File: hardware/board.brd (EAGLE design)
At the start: 100 x 100 mm, 131 parts, among them CON2 USB-FPGA-2THT, IC1 THS3062, IC2 AD80XX, U1 AD9215BRUZ, X1 BU-SMA-V

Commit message: Fully routed ADC
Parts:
- moved CD3 188.6 mm to (48.3, 69.0), flipped to the bottom, turned to 270 degrees
- moved CD4 183.7 mm to (50.7, 69.0), flipped to the bottom, turned to 270 degrees
- moved CD2 176.6 mm to (33.5, 65.2), flipped to the bottom
- moved CR4 176.4 mm to (42.8, 63.1), flipped to the bottom, turned to 90 degrees
- moved CR1 172.0 mm to (39.7, 64.6), flipped to the bottom
- moved CD1 168.1 mm to (33.5, 62.9), flipped to the bottom
- moved CR3 167.2 mm to (36.9, 63.6), flipped to the bottom, turned to 270 degrees
- moved CR2 164.5 mm to (39.7, 62.9), flipped to the bottom
- moved CR5 11.0 mm to (50.1, 64.3), turned to 270 degrees
- moved C22 6.44 mm to (73.6, 69.5), turned to 270 degrees
- moved C12 5.10 mm to (28.5, 65.1), turned to 270 degrees
- moved R9 5.02 mm to (49.6, 75.9), turned to 270 degrees
- moved CF- 3.86 mm to (53.7, 64.3), turned to 180 degrees
- moved CF+ 3.77 mm to (53.7, 71.2), turned to 0 degrees
- moved R20 2.69 mm to (27.8, 75.5), turned to 45 degrees
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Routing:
- net V_ANALOG: track 0.00 -> 85.7 mm, vias 0 -> 7
- net +5V/3: track 48.1 -> 86.7 mm, vias 0 -> 6
- net ADC_CLK: track 0.00 -> 37.6 mm, vias 0 -> 1
- net V_15: track 0.00 -> 36.4 mm, vias 0 -> 3
- net ADC_OR: track 0.00 -> 35.5 mm, vias 0 -> 4
- net ADC_D9: track 0.00 -> 23.9 mm, vias 0 -> 1
- net ADC_D7: track 0.00 -> 23.5 mm, vias 0 -> 1
- net ADC_D8: track 0.00 -> 21.0 mm, vias 0 -> 1
- net ADC_D4: track 0.00 -> 20.0 mm, vias 0 -> 1
- net ADC_D5: track 0.00 -> 19.6 mm, vias 0 -> 1
- net ADC_D3: track 0.00 -> 19.3 mm, vias 0 -> 1
- net ADC_D6: track 0.00 -> 18.9 mm, vias 0 -> 1
- net ADC_IN+: track 0.00 -> 17.2 mm
- net ADC_CLK_FB: track 0.00 -> 17.0 mm, vias 0 -> 1
- net ADC_IN-: track 0.00 -> 16.6 mm, vias 0 -> 2
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- added copper zone on layer 1, net GND2
- added copper zone on layer 16, net GND2

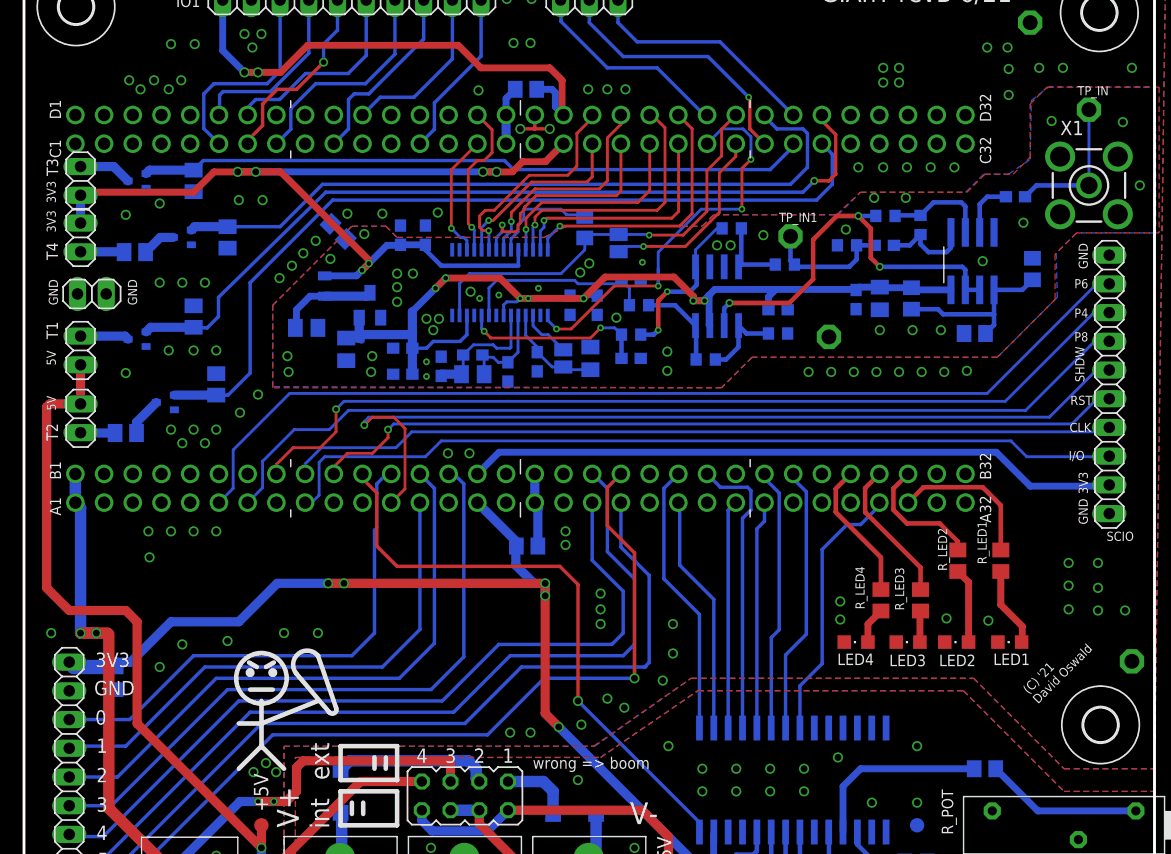
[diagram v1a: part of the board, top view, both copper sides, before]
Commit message: Finalized board, sent to PCBWays
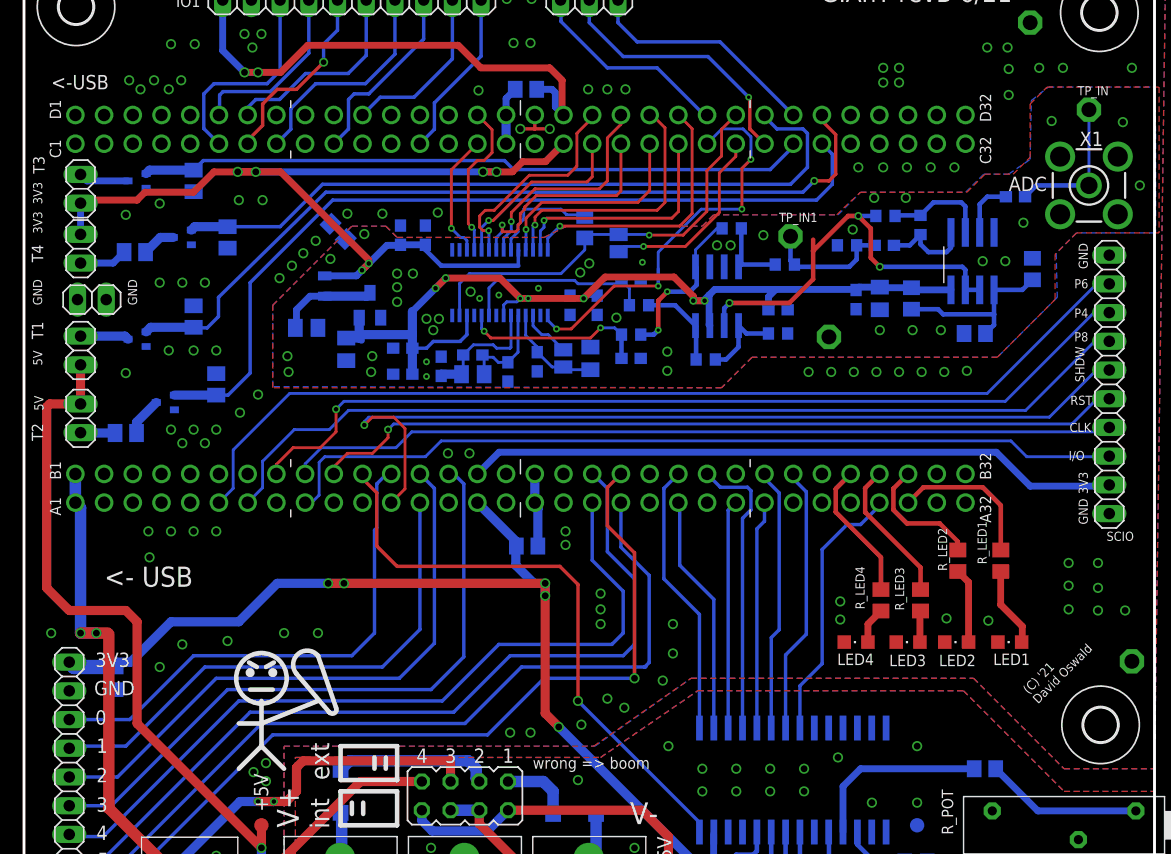
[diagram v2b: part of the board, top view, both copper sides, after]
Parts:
- moved JP5 1.00 mm to (5.00, 74.0)
- moved JP4 0.70 mm to (5.00, 79.3)
- moved JP6 0.50 mm to (6.00, 69.5)
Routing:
- net +5V/3: track 86.7 -> 87.3 mm
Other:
- board text added: "<- USB"
- board text added: "<-USB"
- board text added: "ADC"

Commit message: Board updates Tweaks to LPC First attempt for faultfinder stm32f100
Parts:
- C19: value 10n -> 100n
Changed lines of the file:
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@@
 <attribute name="VALUE" x="0.825" y="38.7" size="1.27" layer="27" rot="R270"/>
 </element>
-<element name="C19" library="rcl" package="C0805K" value="10n" x="8" y="36" smashed="yes" rot="MR270">
+<element name="C19" library="rcl" package="C0805K" value="100n" x="8" y="36" smashed="yes" rot="MR270">
 <attribute name="NAME" x="9.875" y="35" size="1.016" layer="26" rot="MR90"/>
 </element>
